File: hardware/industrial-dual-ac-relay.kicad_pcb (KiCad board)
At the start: 2 copper layers, 40 x 40 mm, 29 parts, among them P1 CON-SENSOR, P2 Digital Output, P3 Debug, P4 Boot, U1 XMC1100, U2 AQH3213AX, U5 AQH3213AX, U6 DRILL, U7 DRILL, U8 DRILL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

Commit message: Data cleanup
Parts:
- U6, U7, U8, U9: footprint kicad-libraries:DRILL_NP -> kicad-libraries:DRILL_NP_New
- moved C2 0.10 mm to (112.1, 44.1)
- moved C3 0.10 mm to (120.0, 44.6)
- moved C4 0.10 mm to (103.2, 46.8)
- moved RP2 0.10 mm to (112.2, 45.8)
- moved R4 0.07 mm to (107.1, 65.1)
- moved P2 0.05 mm to (117.8, 70.0)
- moved R1 0.05 mm to (124.8, 65.1)
- moved G*** 0.05 mm to (127.7, 48.9)
- moved P4 0.05 mm to (101.0, 49.4)
- moved U2 0.05 mm to (123.5, 58.4)
- moved U5 0.05 mm to (105.9, 58.4)
- turned U8 to 90 degrees
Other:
- board text added: "Copyright Tinkerforge GmbH 2023. This documentation describes Open Hardware and is licensed under the CERN OHL v. 1.1. You may redistribute and modify this documentation under the terms of the CERN OHL v.1.1. (http://ohwr.org/cernohl). This documentation is distributed WITHOUT ANY EXPRESS OR IMPLIED WARRANTY, INCLUDING OF MERCHANTABILITY, SATISFACTORY QUALITY AND FITNESS FOR A PARTICULAR PURPOSE.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"
- board text removed: "Copyright Tinkerforge GmbH 2020. This documentation describes Open Hardware and is licensed under the CERN OHL v. 1.1. You may redistribute and modify this documentation under the terms of the CERN OHL v.1.1. (http://ohwr.org/cernohl). This documentation is distributed WITHOUT ANY EXPRESS OR IMPLIED WARRANTY, INCLUDING OF MERCHANTABILITY, SATISFACTORY QUALITY AND FITNESS FOR A PARTICULAR PURPOSE.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"

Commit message: Data cleanup
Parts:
- U7, U8, U9: footprint kicad-libraries:DRILL_NP_New -> kicad-libraries:DRILL_NP
- Ue1: renamed from U6; footprint kicad-libraries:DRILL_NP_New -> kicad-libraries:DRILL_NP
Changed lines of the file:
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@@
   (footprint "kicad-libraries:DEBUG_PAD" (layer "F.Cu")
     (at 101 51)
-    (property "Sheetfile" "C:/Users/tim/tf/industrial-dual-ac-relay-bricklet/hardware/industrial-dual-ac-relay.sch")
+    (property "Sheetfile" "industrial-dual-ac-relay.kicad_sch")
     (property "Sheetname" "")
     (attr through_hole)
@@
   (footprint "kicad-libraries:SolderJumper" (layer "F.Cu")
     (at 101 49.4)
-    (property "Sheetfile" "C:/Users/tim/tf/industrial-dual-ac-relay-bricklet/hardware/industrial-dual-ac-relay.sch")
+    (property "Sheetfile" "industrial-dual-ac-relay.kicad_sch")
     (property "Sheetname" "")
     (attr through_hole)
@@
   (footprint "kicad-libraries:4X0402" (layer "F.Cu")
     (at 112.2 45.8 90)
-    (property "Sheetfile" "C:/Users/tim/tf/industrial-dual-ac-relay-bricklet/hardware/industrial-dual-ac-relay.sch")
+    (property "Sheetfile" "industrial-dual-ac-relay.kicad_sch")
     (property "Sheetname" "")
     (attr smd)
@@
   (footprint "kicad-libraries:C0603F" (layer "F.Cu")
     (at 120 46.2)
-    (property "Sheetfile" "C:/Users/tim/tf/industrial-dual-ac-relay-bricklet/hardware/industrial-dual-ac-relay.sch")
+    (property "Sheetfile" "industrial-dual-ac-relay.kicad_sch")
     (property "Sheetname" "")
     (attr smd)
@@
   (footprint "kicad-libraries:C0402F" (layer "F.Cu")
     (at 112.1 44.1 180)
-    (property "Sheetfile" "C:/Users/tim/tf/industrial-dual-ac-relay-bricklet/hardware/industrial-dual-ac-relay.sch")
+    (property "Sheetfile" "industrial-dual-ac-relay.kicad_sch")
     (property "Sheetname" "")
     (attr through_hole)
@@
   (footprint "kicad-libraries:C0805" (layer "F.Cu")
     (at 120 44.6)
-    (property "Sheetfile" "C:/Users/tim/tf/industrial-dual-ac-relay-bricklet/hardware/industrial-dual-ac-relay.sch")
+    (property "Sheetfile" "industrial-dual-ac-relay.kicad_sch")
     (property "Sheetname" "")
     (attr smd)
@@
   (footprint "kicad-libraries:C0603F" (layer "F.Cu")
     (at 103.2 46.8 90)
-    (property "Sheetfile" "C:/Users/tim/tf/industrial-dual-ac-relay-bricklet/hardware/industrial-dual-ac-relay.sch")
+    (property "Sheetfile" "industrial-dual-ac-relay.kicad_sch")
     (property "Sheetname" "")
     (attr smd)
@@
   (footprint "kicad-libraries:D0603F" (layer "F.Cu")
     (at 108.2 40.5 -90)
-    (property "Sheetfile" "C:/Users/tim/tf/industrial-dual-ac-relay-bricklet/hardware/industrial-dual-ac-relay.sch")
+    (property "Sheetfile" "industrial-dual-ac-relay.kicad_sch")
     (property "Sheetname" "")
     (attr smd)
@@
   (footprint "kicad-libraries:D0603F" (layer "F.Cu")
     (at 129.5 40.5 -90)
-    (property "Sheetfile" "C:/Users/tim/tf/industrial-dual-ac-relay-bricklet/hardware/industrial-dual-ac-relay.sch")
+    (property "Sheetfile" "industrial-dual-ac-relay.kicad_sch")
     (property "Sheetname" "")
     (attr smd)
@@
   (footprint "kicad-libraries:CON-SENSOR2" (layer "F.Cu")
     (at 117.8 38 180)
-    (property "Sheetfile" "C:/Users/tim/tf/industrial-dual-ac-relay-bricklet/hardware/industrial-dual-ac-relay.sch")
+    (property "Sheetfile" "industrial-dual-ac-relay.kicad_sch")
     (property "Sheetname" "")
     (attr through_hole)
@@
   (footprint "kicad-libraries:OQ_8P_230V" (layer "F.Cu")
     (at 117.8 70)
-    (property "Sheetfile" "C:/Users/tim/tf/industrial-dual-ac-relay-bricklet/hardware/industrial-dual-ac-relay.sch")
+    (property "Sheetfile" "industrial-dual-ac-relay.kicad_sch")
     (property "Sheetname" "")
     (attr through_hole)
@@
   (footprint "kicad-libraries:R0603F" (layer "F.Cu")
     (at 106.8 40.5 -90)
-    (property "Sheetfile" "C:/Users/tim/tf/industrial-dual-ac-relay-bricklet/hardware/industrial-dual-ac-relay.sch")
+    (property "Sheetfile" "industrial-dual-ac-relay.kicad_sch")
     (property "Sheetname" "")
     (attr smd)
@@
   (footprint "kicad-libraries:0603X4" (layer "F.Cu")
     (at 115.3 51 180)
-    (property "Sheetfile" "C:/Users/tim/tf/industrial-dual-ac-relay-bricklet/hardware/industrial-dual-ac-relay.sch")
+    (property "Sheetfile" "industrial-dual-ac-relay.kicad_sch")
     (property "Sheetname" "")
     (attr smd)
@@
   (footprint "kicad-libraries:0603X4" (layer "F.Cu")
     (at 128.7 45.1 180)
-    (property "Sheetfile" "C:/Users/tim/tf/industrial-dual-ac-relay-bricklet/hardware/industrial-dual-ac-relay.sch")
+    (property "Sheetfile" "industrial-dual-ac-relay.kicad_sch")
     (property "Sheetname" "")
     (attr smd)
@@
     )
   )
-  (footprint "kicad-libraries:DRILL_NP_New" (layer "F.Cu")
+  (footprint "kicad-libraries:DRILL_NP" (layer "F.Cu")
     (at 100.3 75.5)
-    (property "Sheetfile" "C:/Users/tim/tf/industrial-dual-ac-relay-bricklet/hardware/industrial-dual-ac-relay.sch")
-    (property "Sheetname" "")
-    (fp_text reference "U6" (at 0 -0.5 unlocked) (layer "F.Fab")
+    (property "Sheetfile" "industrial-dual-ac-relay.kicad_sch")
+    (property "Sheetname" "")
+    (fp_text reference "Ue1" (at 0 -0.5 unlocked) (layer "F.Fab")
       (effects (font (size 0.2 0.2) (thickness 0.05)))
     )
@@
       (clearance 0.89))
   )
-  (footprint "kicad-libraries:DRILL_NP_New" (layer "F.Cu")
+  (footprint "kicad-libraries:DRILL_NP" (layer "F.Cu")
     (at 100.3 40.5)
-    (property "Sheetfile" "C:/Users/tim/tf/industrial-dual-ac-relay-bricklet/hardware/industrial-dual-ac-relay.sch")
+    (property "Sheetfile" "industrial-dual-ac-relay.kicad_sch")
     (property "Sheetname" "")
     (fp_text reference "U7" (at 0 -0.5 unlocked) (layer "F.Fab")
@@
       (clearance 0.89))
   )
-  (footprint "kicad-libraries:DRILL_NP_New" (layer "F.Cu")
+  (footprint "kicad-libraries:DRILL_NP" (layer "F.Cu")
     (at 135.3 40.5 90)
-    (property "Sheetfile" "C:/Users/tim/tf/industrial-dual-ac-relay-bricklet/hardware/industrial-dual-ac-relay.sch")
+    (property "Sheetfile" "industrial-dual-ac-relay.kicad_sch")
     (property "Sheetname" "")
     (fp_text reference "U8" (at 0 -0.5 90 unlocked) (layer "F.Fab")
@@
       (clearance 0.89))
   )
-  (footprint "kicad-libraries:DRILL_NP_New" (layer "F.Cu")
+  (footprint "kicad-libraries:DRILL_NP" (layer "F.Cu")
     (at 135.3 75.5)
-    (property "Sheetfile" "C:/Users/tim/tf/industrial-dual-ac-relay-bricklet/hardware/industrial-dual-ac-relay.sch")
+    (property "Sheetfile" "industrial-dual-ac-relay.kicad_sch")
     (property "Sheetname" "")
     (fp_text reference "U9" (at 0 -0.5 unlocked) (layer "F.Fab")
@@
   (footprint "kicad-libraries:VAR_10mm" (layer "F.Cu")
     (at 107.1 65.1 180)
-    (property "Sheetfile" "C:/Users/tim/tf/industrial-dual-ac-relay-bricklet/hardware/industrial-dual-ac-relay.sch")
+    (property "Sheetfile" "industrial-dual-ac-relay.kicad_sch")
     (property "Sheetname" "")
     (attr through_hole)
@@
   (footprint "kicad-libraries:0603X4" (layer "F.Cu")
     (at 120.3 51 180)
-    (property "Sheetfile" "C:/Users/tim/tf/industrial-dual-ac-relay-bricklet/hardware/industrial-dual-ac-relay.sch")
+    (property "Sheetfile" "industrial-dual-ac-relay.kicad_sch")
     (property "Sheetname" "")
     (attr smd)
@@
   (footprint "kicad-libraries:AQ-H" (layer "F.Cu")
     (at 105.9 58.4 180)
-    (property "Sheetfile" "C:/Users/tim/tf/industrial-dual-ac-relay-bricklet/hardware/industrial-dual-ac-relay.sch")
+    (property "Sheetfile" "industrial-dual-ac-relay.kicad_sch")
     (property "Sheetname" "")
     (attr through_hole)
@@
   (footprint "kicad-libraries:D0603F" (layer "F.Cu")
     (at 127.9 40.5 -90)
-    (property "Sheetfile" "C:/Users/tim/tf/industrial-dual-ac-relay-bricklet/hardware/industrial-dual-ac-relay.sch")
+    (property "Sheetfile" "industrial-dual-ac-relay.kicad_sch")
     (property "Sheetname" "")
     (attr smd)
@@
     (at 106.8 46.8 -90)
     (tags "QFN 24pin 0.5")
-    (property "Sheetfile" "C:/Users/tim/tf/industrial-dual-ac-relay-bricklet/hardware/industrial-dual-ac-relay.sch")
+    (property "Sheetfile" "industrial-dual-ac-relay.kicad_sch")
     (property "Sheetname" "")
     (attr smd)
@@
   (footprint "kicad-libraries:VAR_10mm" (layer "F.Cu")
     (at 124.8 65.1 180)
-    (property "Sheetfile" "C:/Users/tim/tf/industrial-dual-ac-relay-bricklet/hardware/industrial-dual-ac-relay.sch")
+    (property "Sheetfile" "industrial-dual-ac-relay.kicad_sch")
     (property "Sheetname" "")
     (attr through_hole)
@@
   (footprint "kicad-libraries:AQ-H" (layer "F.Cu")
     (at 123.5 58.4 180)
-    (property "Sheetfile" "C:/Users/tim/tf/industrial-dual-ac-relay-bricklet/hardware/industrial-dual-ac-relay.sch")
-    (property "Sheetname" "")
-    (attr through_hole)
+    (property "Sheetfile" "industrial-dual-ac-relay.kicad_sch")
+    (property "Sheetname" "")
+    (attr through_hole)

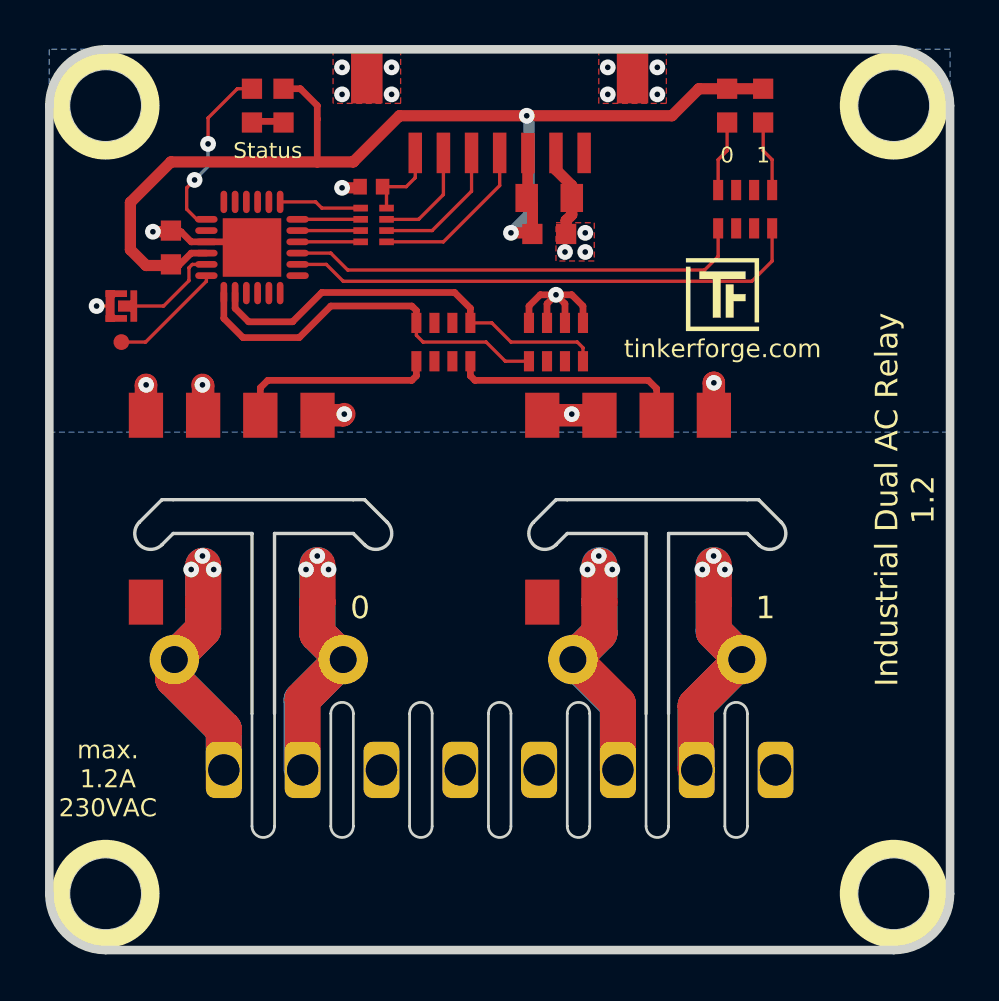
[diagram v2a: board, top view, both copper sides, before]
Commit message: added fiducials
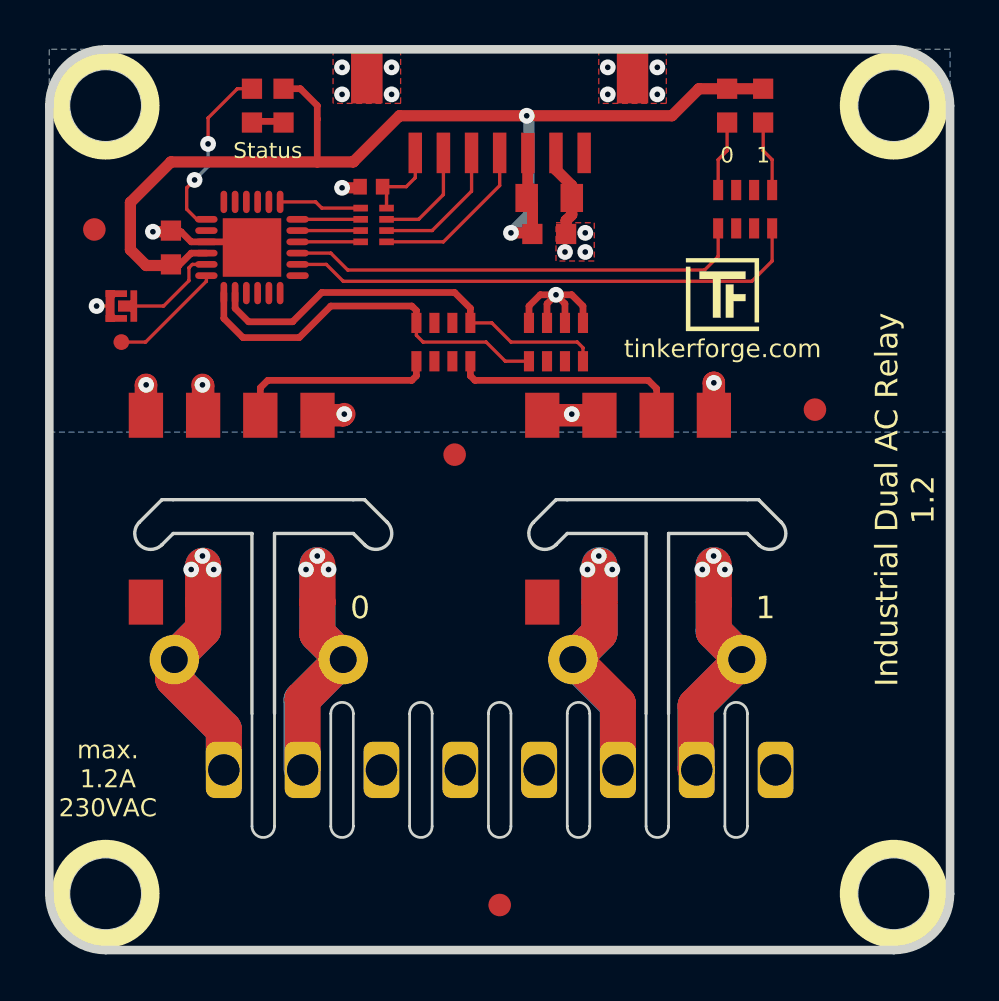
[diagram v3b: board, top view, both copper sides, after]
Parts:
- added Fiducial_Mark: VAL**, kicad-libraries:Fiducial_Mark, F.Cu at (115.8, 56.0)
- added Fiducial_Mark: VAL**, kicad-libraries:Fiducial_Mark, F.Cu at (117.8, 76.0)
- added Fiducial_Mark: VAL**, kicad-libraries:Fiducial_Mark, F.Cu at (99.8, 46.0)
- added Fiducial_Mark: VAL**, kicad-libraries:Fiducial_Mark, F.Cu at (131.8, 54.0)
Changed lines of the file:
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@@
       ) (layer "F.SilkS") (width 0.01) (fill solid))
+  )
+  (footprint "kicad-libraries:Fiducial_Mark" (layer "F.Cu")
+    (at 115.8 56)
+    (attr smd)
+    (fp_text reference "Fiducial_Mark" (at 0 0) (layer "F.SilkS") hide
+      (effects (font (size 0.127 0.127) (thickness 0.03302)))
+    )
+    (fp_text value "VAL**" (at 0 -0.29972) (layer "F.SilkS") hide
+      (effects (font (size 0.127 0.127) (thickness 0.03302)))
+    )
+    (fp_circle (center 0 0) (end 1.15062 0) (layer "Dwgs.User") (width 0.01016) (fill none))
+    (pad "1" smd circle locked (at 0 0) (size 1.00076 1.00076) (layers "F.Cu" "F.Paste" "F.Mask")
+      (clearance 0.65024))
+  )
+  (footprint "kicad-libraries:Fiducial_Mark" (layer "F.Cu")
+    (at 117.8 76)
+    (attr smd)
+    (fp_text reference "Fiducial_Mark" (at 0 0) (layer "F.SilkS") hide
+      (effects (font (size 0.127 0.127) (thickness 0.03302)))
+    )
+    (fp_text value "VAL**" (at 0 -0.29972) (layer "F.SilkS") hide
+      (effects (font (size 0.127 0.127) (thickness 0.03302)))
+    )
+    (fp_circle (center 0 0) (end 1.15062 0) (layer "Dwgs.User") (width 0.01016) (fill none))
+    (pad "1" smd circle locked (at 0 0) (size 1.00076 1.00076) (layers "F.Cu" "F.Paste" "F.Mask")
+      (clearance 0.65024))
+  )
+  (footprint "kicad-libraries:Fiducial_Mark" (layer "F.Cu")
+    (at 99.8 46)
+    (attr smd)
+    (fp_text reference "Fiducial_Mark" (at 0 0) (layer "F.SilkS") hide
+      (effects (font (size 0.127 0.127) (thickness 0.03302)))
+    )
+    (fp_text value "VAL**" (at 0 -0.29972) (layer "F.SilkS") hide
+      (effects (font (size 0.127 0.127) (thickness 0.03302)))
+    )
+    (fp_circle (center 0 0) (end 1.15062 0) (layer "Dwgs.User") (width 0.01016) (fill none))
+    (pad "1" smd circle locked (at 0 0) (size 1.00076 1.00076) (layers "F.Cu" "F.Paste" "F.Mask")
+      (clearance 0.65024))
+  )
+  (footprint "kicad-libraries:Fiducial_Mark" (layer "F.Cu")
+    (at 131.8 54)
+    (attr smd)
+    (fp_text reference "Fiducial_Mark" (at 0 0) (layer "F.SilkS") hide
+      (effects (font (size 0.127 0.127) (thickness 0.03302)))
+    )
+    (fp_text value "VAL**" (at 0 -0.29972) (layer "F.SilkS") hide
+      (effects (font (size 0.127 0.127) (thickness 0.03302)))
+    )
+    (fp_circle (center 0 0) (end 1.15062 0) (layer "Dwgs.User") (width 0.01016) (fill none))
+    (pad "1" smd circle locked (at 0 0) (size 1.00076 1.00076) (layers "F.Cu" "F.Paste" "F.Mask")
+      (clearance 0.65024))
   )
   (footprint "kicad-libraries:WEEE_7mm" (layer "B.Cu")
